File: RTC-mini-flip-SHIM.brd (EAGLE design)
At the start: 17.8 x 20.3 mm, 10 parts, among them IC1 DS3231/SO

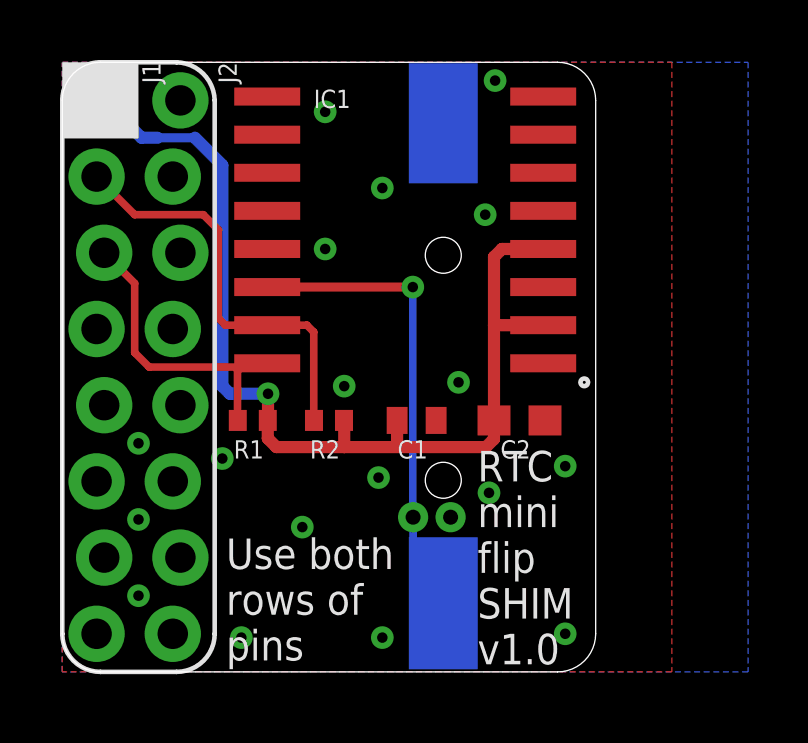
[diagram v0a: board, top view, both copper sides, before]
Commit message: Add battery connector to the front of mini SHIM too. Generate new CAM.
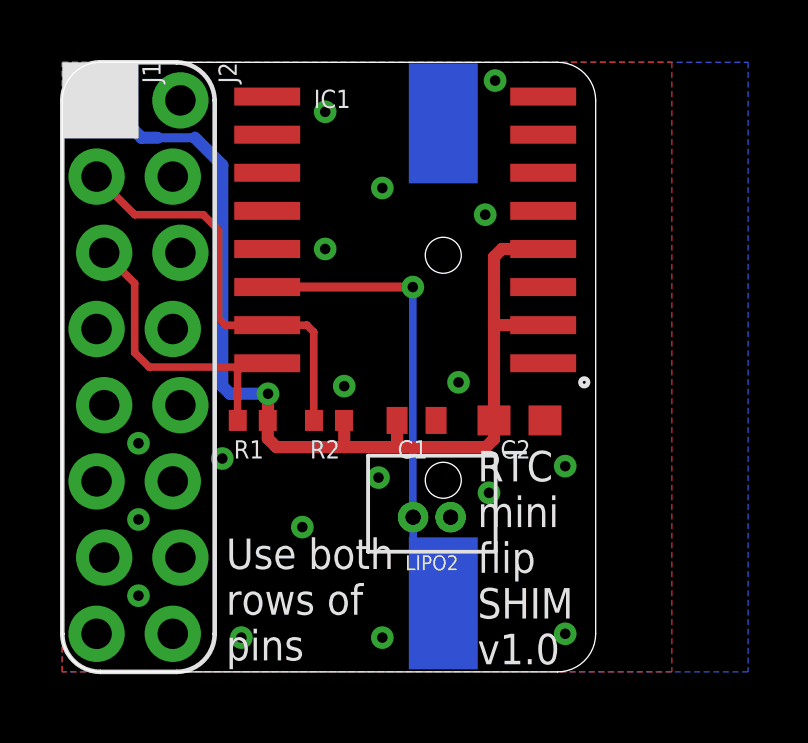
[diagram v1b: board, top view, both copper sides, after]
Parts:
- added LIPO2: Molex VERT 1.25mm pitch, PiB_connectors:_MOLEX-0530470210_VERT_PITCH-1.25MM
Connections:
- net GND: now also LIPO2.2
- net VBAT: now also LIPO2.1
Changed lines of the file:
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@@
 <attribute name="VALUE" x="12.319" y="4.3942" size="0.25" layer="28" font="vector" ratio="10" rot="MR180" align="bottom-center"/>
+</element>
+<element name="LIPO2" library="PiB_connectors" package="_MOLEX-0530470210_VERT_PITCH-1.25MM" package3d_urn="urn:adsk.eagle:package:2973718/3" value="Molex VERT 1.25mm pitch" x="12.319" y="5.1562" smashed="yes">
+<attribute name="DATASHEET_CONNECTOR1" value="https://www.molex.com/pdm_docs/sd/530470210_sd.pdf" x="12.319" y="5.1562" size="1.778" layer="27" display="off"/>
+<attribute name="DATASHEET_CONNECTOR2" value="https://www.molex.com/pdm_docs/sd/510210700_sd.pdf" x="12.319" y="5.1562" size="1.778" layer="27" display="off"/>
+<attribute name="DATASHEET_CRIMP" value="https://www.molex.com/pdm_docs/sd/500798000_sd.pdf" x="12.319" y="5.1562" size="1.778" layer="27" display="off"/>
+<attribute name="DISTLINK_CONNECTOR1" value="https://www.digikey.com/products/en?keywords=WM1731-ND" x="12.319" y="5.1562" size="1.778" layer="27" display="off"/>
+<attribute name="DISTLINK_CONNECTOR2" value="https://www.digikey.com/products/en?keywords=WM1720-ND" x="12.319" y="5.1562" size="1.778" layer="27" display="off"/>
+<attribute name="DISTLINK_CRIMP" value="https://www.digikey.com/products/en?keywords=WM1142CT-ND" x="12.319" y="5.1562" size="1.778" layer="27" display="off"/>
+<attribute name="DISTPN_CONNECTOR1" value="WM1731-ND" x="12.319" y="5.1562" size="1.778" layer="27" display="off"/>
+<attribute name="DISTPN_CONNECTOR2" value="WM1720-ND" x="12.319" y="5.1562" size="1.778" layer="27" display="off"/>
+<attribute name="DISTPN_CRIMP" value="WM1142CT-ND" x="12.319" y="5.1562" size="1.778" layer="27" display="off"/>
+<attribute name="DIST_CONNECTOR1" value="Digikey" x="12.319" y="5.1562" size="1.778" layer="27" display="off"/>
+<attribute name="DIST_CONNECTOR2" value="Digikey" x="12.319" y="5.1562" size="1.778" layer="27" display="off"/>
+<attribute name="DIST_CRIMP" value="Digikey" x="12.319" y="5.1562" size="1.778" layer="27" display="off"/>
+<attribute name="MFR_CONNECTOR1" value="Molex, LLC" x="12.319" y="5.1562" size="1.778" layer="27" display="off"/>
+<attribute name="MFR_CONNECTOR2" value="Molex, LLC" x="12.319" y="5.1562" size="1.778" layer="27" display="off"/>
+<attribute name="MFR_CRIMP" value="Molex, LLC" x="12.319" y="5.1562" size="1.778" layer="27" display="off"/>
+<attribute name="MPN_CONNECTOR1" value="0530470210" x="12.319" y="5.1562" size="1.778" layer="27" display="off"/>
+<attribute name="MPN_CONNECTOR2" value="51021-0200" x="12.319" y="5.1562" size="1.778" layer="27" display="off"/>
+<attribute name="MPN_CRIMP" value="0500798000" x="12.319" y="5.1562" size="1.778" layer="27" display="off"/>
+<attribute name="NAME" x="12.319" y="3.8862" size="0.5" layer="25" font="vector" ratio="10" align="top-center"/>
+<attribute name="VALUE" x="12.319" y="5.9182" size="0.25" layer="27" font="vector" ratio="10" align="bottom-center"/>
 </element>
 </elements>
@@
 <wire x1="11.694" y1="5.1562" x2="11.694" y2="3.293" width="0.254" layer="16"/>
 <wire x1="11.694" y1="3.293" x2="12.7" y2="2.287" width="0.254" layer="16"/>
+<contactref element="LIPO2" pad="1"/>
 </signal>
 <signal name="SCL">
@@
 <via x="14.4272" y="19.7104" extent="1-16" drill="0.35"/>
 <contactref element="LIPO1" pad="2"/>
+<contactref element="LIPO2" pad="2"/>
 </signal>
 </signals>
